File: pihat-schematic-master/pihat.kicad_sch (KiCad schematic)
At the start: 6 parts, among them J1 Raspberry_Pi_2_3, J2 2601-3114, J3 2601-3114

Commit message: Updates to Pihat
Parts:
- removed 3V3_Connection1, 5V_Connection1: Screw_Terminal_01x06, TerminalBlock_Phoenix:TerminalBlock_Phoenix_MKDS-1,5-5-5.08_1x05_P5.08mm_Horizontal, symbol Connector:Screw_Terminal_01x05
- removed Ground_connection1: Screw_Terminal_01x9, TerminalBlock_Altech:Altech_AK300_1x10_P5.00mm_45-Degree, symbol Connector:Screw_Terminal_01x10
- added J4: 5V_Connect, wago_terms:CONN5_2601-3105_WAG, symbol Wago2:2601-3105
- added J5: 3V_Connect, wago_terms:CONN5_2601-3105_WAG, symbol Wago2:2601-3105
- added J6: 2601-1110, wago_terms:CONN10_2601-1110_WAG, symbol Wago4:2601-1110
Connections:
- net at J1.1 (3V3), J1.17 (3V3): now also J5.1 (1_1), J5.10 (5_2), J5.2 (1_2), J5.3 (2_1), J5.4 (2_2), J5.5 (3_1), J5.6 (3_2), J5.7 (4_1), J5.8 (4_2), J5.9 (5_1)
- net at J1.14 (GND), J1.20 (GND), J1.25 (GND)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: now also J6.1 (1_1), J6.10 (5_2), J6.11 (6_1), J6.12 (6_2), J6.13 (7_1), J6.14 (7_2), J6.15 (8_1), J6.16 (8_2), J6.17 (9_1), J6.18 (9_2), J6.19 (10_1), J6.2 (1_2), J6.20 (10_2), J6.3 (2_1), J6.4 (2_2), J6.5 (3_1), J6.6 (3_2), J6.7 (4_1), J6.8 (4_2), J6.9 (5_1)
- net at J1.2 (5V), J1.4 (5V): now also J4.1 (1_1), J4.10 (5_2), J4.2 (1_2), J4.3 (2_1), J4.4 (2_2), J4.5 (3_1), J4.6 (3_2), J4.7 (4_1), J4.8 (4_2), J4.9 (5_1)

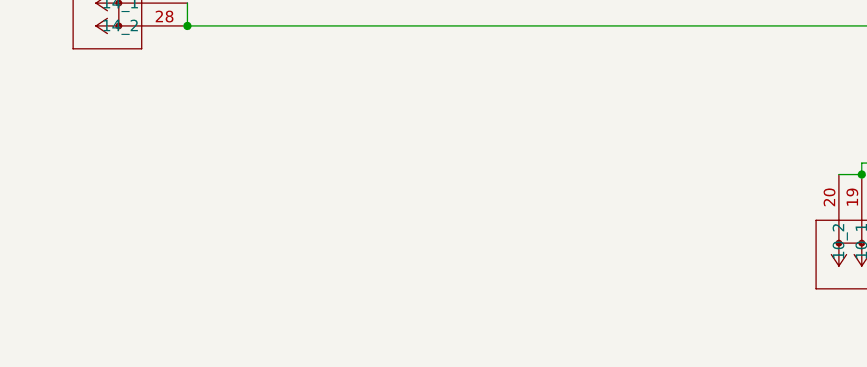
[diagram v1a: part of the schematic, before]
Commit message: Began adding breakout pins
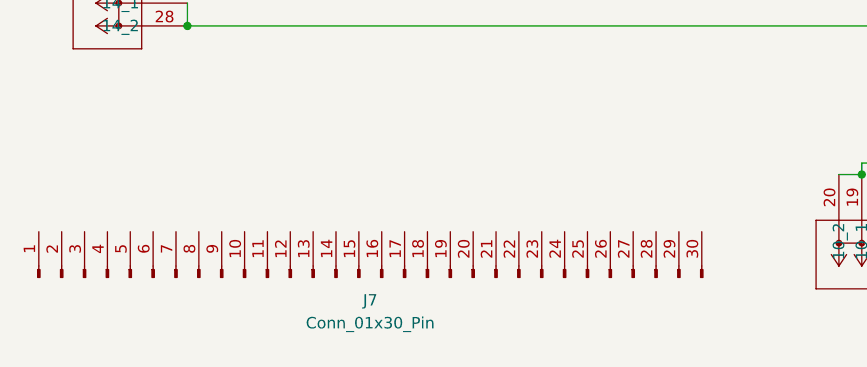
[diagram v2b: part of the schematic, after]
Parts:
- added J7: Conn_01x30_Pin, symbol Connector:Conn_01x30_Pin
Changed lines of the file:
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@@
+	)
+	(symbol
+		(lib_id "Connector:Conn_01x30_Pin")
+		(at 91.44 166.37 90)
+		(unit 1)
+		(exclude_from_sim no)
+		(in_bom yes)
+		(on_board yes)
+		(dnp no)
+		(fields_autoplaced yes)
+		(property "Reference" "J7"
+			(at 92.71 168.91 90)
+			(effects
+				(font
+					(size 1.27 1.27)
+				)
+			)
+		)
+		(property "Value" "Conn_01x30_Pin"
+			(at 92.71 171.45 90)
+			(effects
+				(font
+					(size 1.27 1.27)
+				)
+			)
+		)
+		(property "Footprint" ""
+			(at 91.44 166.37 0)
+			(effects
+				(font
+					(size 1.27 1.27)
+				)
+				(hide yes)
+			)
+		)
+		(property "Datasheet" "~"
+			(at 91.44 166.37 0)
+			(effects
+				(font
+					(size 1.27 1.27)
+				)
+				(hide yes)
+			)
+		)
+		(property "Description" "Generic connector, single row, 01x30, script generated"
+			(at 91.44 166.37 0)
+			(effects
+				(font
+					(size 1.27 1.27)
+				)
+				(hide yes)
+			)
+		)
+		(pin "19"
+		)
+		(pin "28"
+		)
+		(pin "10"
+		)
+		(pin "11"
+		)
+		(pin "8"
+		)
+		(pin "7"
+		)
+		(pin "20"
+		)
+		(pin "26"
+		)
+		(pin "2"
+		)
+		(pin "29"
+		)
+		(pin "1"
+		)
+		(pin "23"
+		)
+		(pin "4"
+		)
+		(pin "6"
+		)
+		(pin "22"
+		)
+		(pin "24"
+		)
+		(pin "27"
+		)
+		(pin "21"
+		)
+		(pin "13"
+		)
+		(pin "9"
+		)
+		(pin "12"
+		)
+		(pin "18"
+		)
+		(pin "17"
+		)
+		(pin "3"
+		)
+		(pin "14"
+		)
+		(pin "5"
+		)
+		(pin "15"
+		)
+		(pin "25"
+		)
+		(pin "30"
+		)
+		(pin "16"
+		)
+		(instances
+			(project ""
+				(path "/9edb751a-cfae-4d00-8cfd-9bdb2570cfc8"
+					(reference "J7")
+					(unit 1)
+				)
+			)
+		)
 	)
 	(symbol
